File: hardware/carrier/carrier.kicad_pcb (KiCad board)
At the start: 4 copper layers, 24 x 70 mm, 4 parts

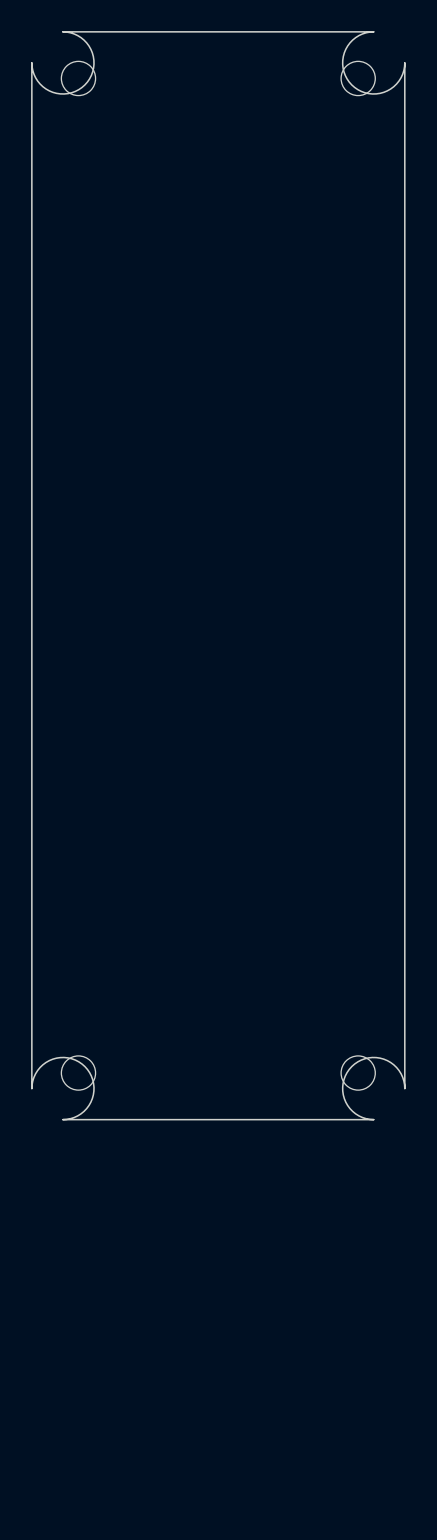
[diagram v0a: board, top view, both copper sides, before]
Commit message: feat(hardware): nets, XIAO headers and inner planes; board 24x70 -> 24x95
Stage 2b, partially. DRC clean at 0 violations, 0 unconnected -- and that
result now means something, because the board has a netlist to check. Before
this it was decorative copper and "0 unconnected" was vacuous.

The board had to grow. 70 mm assumed the two XIAOs could overlap in plan view,
one per face. They cannot: these are through-hole headers so the holes pass
through the board, and XIAO A uses D6/D7 for the GPS UART while XIAO B uses
D4/D5 for I2C -- different nets on the same holes. End to end, the bottom face
needs XIAO 21 + LSM6DSO32 25.5 + BMP390 25.5 + buzzer, about 84 mm, and at
24 mm wide against 17.8 mm sensors nothing sits side by side. 95 mm covers it
for 1.1 g, and still lands inside the 150 mm sled with 36 mm to spare.

GND on In1 and +3V3 on In2 as filled planes. That is what the 4-layer stackup
was for: the two XIAOs share power and ground with no routed trace, and every
future signal gets a solid return path beneath it. Verified from the exported
gerbers -- inner layers are ~39 KB against 2 KB for the empty outer layers, so
the fills are real rather than empty zone outlines.

Caught an off-by-one in my own pin mapping before it reached copper. The KiCad
footprint numbers pads 1..14 with no names; Seeed's pinout makes 1..7 = D0..D6
and 8..14 = D7, D8, D9, D10, 3V3, GND, 5V. GPS had been on pins 6/7 and I2C on
4/5 -- D5/D6 and D3/D4, every one wrong by one. Found by reading the mapping
back out of the saved board rather than trusting the generator's own output.
Pins are now named, so the numbers never appear by hand.

GPS, sensor, buzzer and battery-JST footprints are deliberately absent. Their
header pin ORDER varies by vendor and a wrong order scraps a board rather than
costing a re-solder. They land once the breadboard confirms the parts in hand.

Co-Authored-By: Claude Opus 5 <noreply@anthropic.com>
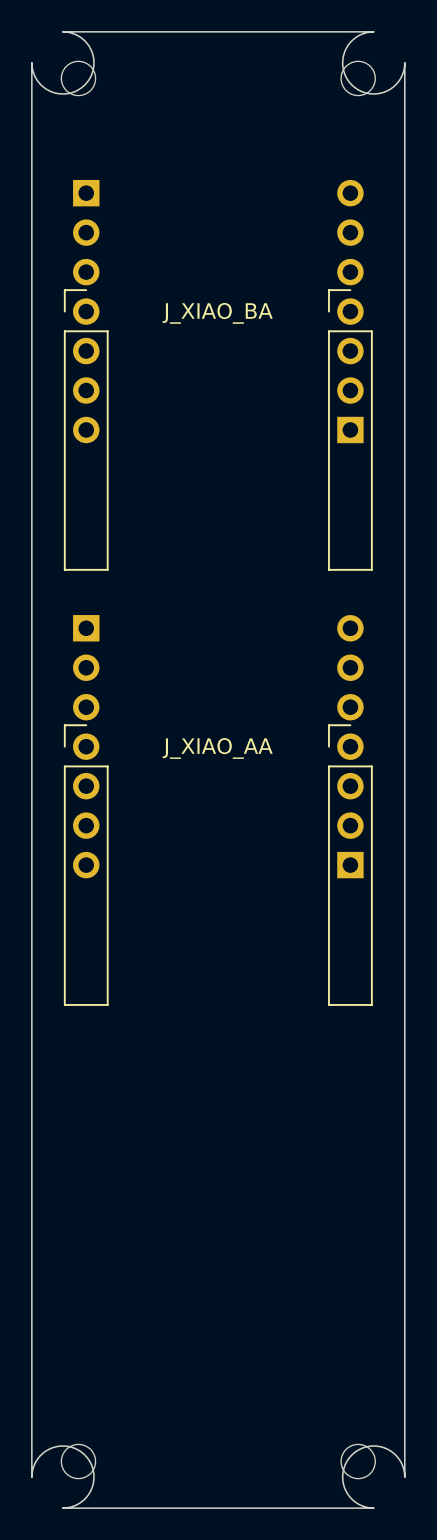
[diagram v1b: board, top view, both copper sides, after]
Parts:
- added J_XIAO_AA: PinHeader_1x07_P2.54mm_Vertical, PinHeader_1x07_P2.54mm_Vertical, F.Cu at (3.50, 46.0)
- added J_XIAO_AB: PinHeader_1x07_P2.54mm_Vertical, PinHeader_1x07_P2.54mm_Vertical, F.Cu at (20.5, 46.0)
- added J_XIAO_BA: PinHeader_1x07_P2.54mm_Vertical, PinHeader_1x07_P2.54mm_Vertical, F.Cu at (3.50, 18.0)
- added J_XIAO_BB: PinHeader_1x07_P2.54mm_Vertical, PinHeader_1x07_P2.54mm_Vertical, F.Cu at (20.5, 18.0)
- moved H3 25.0 mm to (3.00, 92.0)
- moved H4 25.0 mm to (21.0, 92.0)
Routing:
- added copper zone on In2.Cu, net +3V3
- added copper zone on In1.Cu, net GND
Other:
- board size 24 x 70 mm -> 24 x 95 mm
